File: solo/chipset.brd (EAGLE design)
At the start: 41 x 15 mm, 24 parts

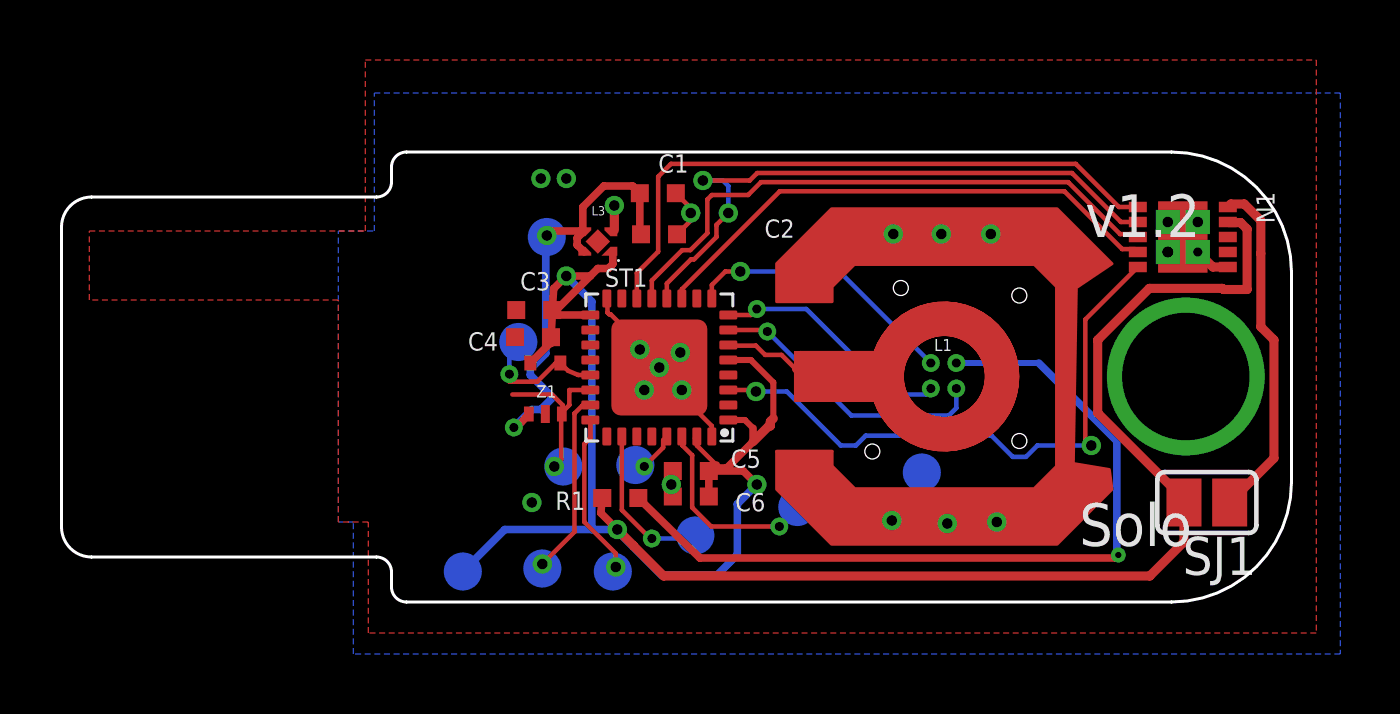
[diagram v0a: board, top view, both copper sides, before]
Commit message: add molex nfc antenna/coil
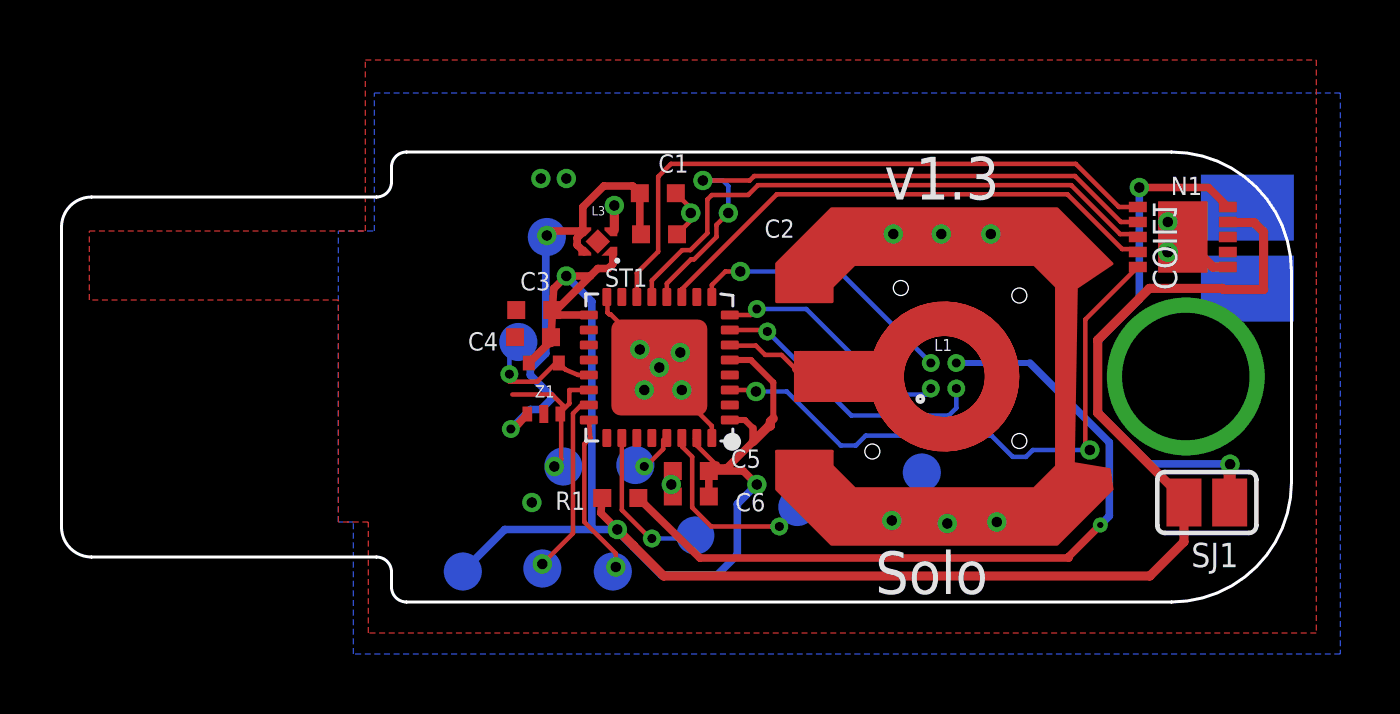
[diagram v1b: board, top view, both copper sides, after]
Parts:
- added COIL1: MOLEX_NFC_COIL_1462360101, efm-fido:MOLEX_NFC_COIL1
- moved Z1 0.05 mm to (50.5, 53.0)
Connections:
- new net N$12: N1.P$4
- new net N$13: N1.P$3
- net PE: no longer N1.P$12, N1.P$13, N1.P$14, N1.P$15
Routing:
- net N$7: track 11.6 -> 17.7 mm, vias 0 -> 2
- net N$6: track 27.2 -> 25.9 mm
- net +3V3: track 80.0 -> 80.9 mm
- net PE: track 18.6 -> 18.7 mm, vias 21 -> 20
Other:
- board text added: "v1.3"
- board text removed: "v1.2"

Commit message: update chipset
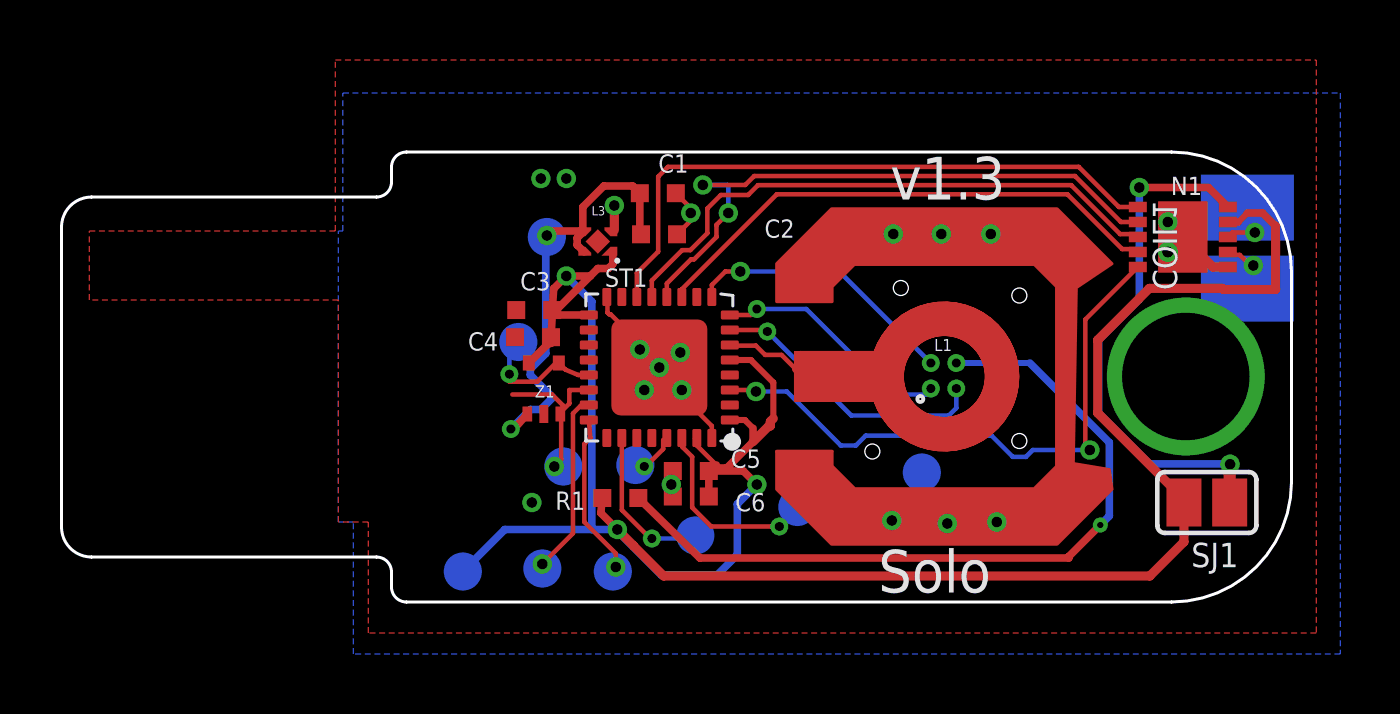
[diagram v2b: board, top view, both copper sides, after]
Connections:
- net N$12: now also COIL1.P$2
- net N$13: now also COIL1.P$1
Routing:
- net N$13: track 0.00 -> 1.90 mm, vias 0 -> 1
- net N$12: track 0.00 -> 1.89 mm, vias 0 -> 1
- net +3V3: track 80.9 -> 82.1 mm
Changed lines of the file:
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@@
 <plain>
 <wire x1="74.05" y1="54.25" x2="35.1" y2="54.25" width="0.1524" layer="49"/>
-<text x="62.1" y="47" size="1.4224" layer="21">Solo</text>
-<text x="62.4" y="60.15" size="1.4224" layer="21">v1.3</text>
+<text x="62.2" y="47.05" size="1.4224" layer="21">Solo</text>
+<text x="62.6" y="60.15" size="1.4224" layer="21">v1.3</text>
 <hole x="62" y="51.75" drill="0.5"/>
 <wire x1="35" y1="59.3" x2="45.9" y2="59.3" width="0.2" layer="47"/>
@@
 <vertex x="35.9" y="56.8"/>
 <vertex x="35.9" y="59.1"/>
-<vertex x="45.1" y="59.1"/>
-<vertex x="45.1" y="64.8"/>
+<vertex x="44.1" y="59.1"/>
+<vertex x="44.1" y="64.8"/>
 <vertex x="76.8" y="64.8"/>
-<vertex x="76.8" y="57.5"/>
 <vertex x="76.8" y="45.7"/>
 <vertex x="45.2" y="45.7"/>
@@
 <polygon width="0.1016" layer="16">
 <vertex x="44.2" y="59.1"/>
-<vertex x="45.4" y="59.1"/>
-<vertex x="45.4" y="63.7"/>
+<vertex x="44.35" y="59.1"/>
+<vertex x="44.35" y="63.7"/>
 <vertex x="77.6" y="63.7"/>
 <vertex x="77.6" y="45"/>
@@
 <wire x1="71.25" y1="47.6" x2="72.388" y2="48.738" width="0.3048" layer="1"/>
 <wire x1="72.388" y1="48.738" x2="72.388" y2="50.05" width="0.3048" layer="1"/>
-<wire x1="73.8702" y1="59.3798" x2="74.72625" y2="59.3798" width="0.3048" layer="1"/>
-<wire x1="74.72625" y1="59.3798" x2="75.0428" y2="59.06325" width="0.3048" layer="1"/>
-<wire x1="75.0428" y1="59.06325" x2="75.0428" y2="57.15" width="0.3048" layer="1"/>
+<wire x1="75.4428" y1="59.26325" x2="75.4428" y2="57.15" width="0.3048" layer="1"/>
 <wire x1="73.66688125" y1="57.1878" x2="71.23311875" y2="57.1878" width="0.3048" layer="1"/>
 <wire x1="71.23311875" y1="57.1878" x2="69.5122" y2="55.46688125" width="0.3048" layer="1"/>
 <wire x1="69.5122" y1="55.46688125" x2="69.5122" y2="53.03311875" width="0.3048" layer="1"/>
-<wire x1="75.0428" y1="57.15" x2="73.70468125" y2="57.15" width="0.3048" layer="1"/>
+<wire x1="75.4428" y1="57.15" x2="73.70468125" y2="57.15" width="0.3048" layer="1"/>
 <wire x1="73.70468125" y1="57.15" x2="73.66688125" y2="57.1878" width="0.3048" layer="1"/>
 <wire x1="72.388" y1="50.15731875" x2="72.388" y2="50.05" width="0.3048" layer="1"/>
 <wire x1="69.5122" y1="53.03311875" x2="72.388" y2="50.15731875" width="0.3048" layer="1"/>
-<wire x1="73.85" y1="59.4" x2="73.8702" y2="59.3798" width="0.1524" layer="1"/>
+<wire x1="73.85" y1="59.4" x2="73.8798" y2="59.4298" width="0.254" layer="1"/>
+<wire x1="73.85" y1="59.4" x2="74.2" y2="59.4" width="0.254" layer="1"/>
+<wire x1="74.2" y1="59.4" x2="74.5" y2="59.7" width="0.2032" layer="1"/>
+<wire x1="74.5" y1="59.7" x2="75.00605" y2="59.7" width="0.254" layer="1"/>
+<wire x1="75.00605" y1="59.7" x2="75.4428" y2="59.26325" width="0.254" layer="1"/>
 </signal>
 <signal name="N$6">
@@
 <wire x1="70.7536" y1="58.9964" x2="70.2597125" y2="58.9964" width="0.1524" layer="1"/>
 <wire x1="70.2597125" y1="58.9964" x2="68.6279125" y2="60.6282" width="0.1524" layer="1"/>
-<wire x1="57.861175" y1="60.3" x2="56.65" y2="60.3" width="0.1524" layer="1"/>
-<wire x1="56.65" y1="60.3" x2="56.5" y2="60.15" width="0.1524" layer="1"/>
+<wire x1="57.861175" y1="60.3" x2="56.95" y2="60.3" width="0.1524" layer="1"/>
+<wire x1="56.95" y1="60.3" x2="56.5" y2="59.85" width="0.1524" layer="1"/>
 <wire x1="58.189375" y1="60.6282" x2="57.861175" y2="60.3" width="0.1524" layer="1"/>
 <wire x1="55.9346875" y1="58.4614" x2="55.6614" y2="58.4614" width="0.1524" layer="1"/>
 <wire x1="56.5" y1="59.0267125" x2="55.9346875" y2="58.4614" width="0.1524" layer="1"/>
 <wire x1="54.65" y1="57.45" x2="54.65" y2="56.9" width="0.1524" layer="1"/>
-<wire x1="56.5" y1="60.15" x2="56.5" y2="59.0267125" width="0.1524" layer="1"/>
+<wire x1="56.5" y1="59.85" x2="56.5" y2="59.0267125" width="0.1524" layer="1"/>
 <wire x1="55.6614" y1="58.4614" x2="54.65" y2="57.45" width="0.1524" layer="1"/>
 </signal>
@@
 <wire x1="70.28716875" y1="59.4" x2="68.75416875" y2="60.933" width="0.1524" layer="1"/>
 <wire x1="68.75416875" y1="60.933" x2="58.06311875" y2="60.933" width="0.1524" layer="1"/>
-<wire x1="58.06311875" y1="60.933" x2="57.91431875" y2="60.7842" width="0.1524" layer="1"/>
-<wire x1="57.91431875" y1="60.7842" x2="56.3512875" y2="60.7842" width="0.1524" layer="1"/>
-<via x="56.3512875" y="60.7842" extent="1-16" drill="0.35"/>
-<wire x1="56.3512875" y1="60.7842" x2="57.0158" y2="60.7842" width="0.1524" layer="16"/>
-<wire x1="57.0158" y1="60.7842" x2="57.2" y2="60.6" width="0.1524" layer="16"/>
+<wire x1="58.06311875" y1="60.933" x2="57.76431875" y2="60.6342" width="0.1524" layer="1"/>
+<wire x1="57.76431875" y1="60.6342" x2="56.3512875" y2="60.6342" width="0.1524" layer="1"/>
+<via x="56.3512875" y="60.6342" extent="1-16" drill="0.35"/>
+<wire x1="56.3512875" y1="60.6342" x2="57.1658" y2="60.6342" width="0.1524" layer="16"/>
+<wire x1="57.1658" y1="60.6342" x2="57.2" y2="60.6" width="0.1524" layer="16"/>
 <wire x1="57.2" y1="60.6" x2="57.2" y2="59.7" width="0.1524" layer="16"/>
 <via x="57.2" y="59.7" extent="1-16" drill="0.35"/>
@@
 <contactref element="ST1" pad="14"/>
 <wire x1="70.85" y1="59.9" x2="70.218225" y2="59.9" width="0.1524" layer="1"/>
-<wire x1="68.780425" y1="61.3378" x2="70.218225" y2="59.9" width="0.1524" layer="1"/>
+<wire x1="68.880425" y1="61.2378" x2="70.218225" y2="59.9" width="0.1524" layer="1"/>
 <wire x1="54.15" y1="57.7" x2="54.15" y2="56.9" width="0.1524" layer="1"/>
 <wire x1="54.15" y1="57.7" x2="54.8614" y2="58.4114" width="0.1524" layer="1"/>
 <wire x1="54.8614" y1="58.4114" x2="54.8614" y2="60.9114" width="0.1524" layer="1"/>
-<wire x1="54.8614" y1="60.9114" x2="55.2878" y2="61.3378" width="0.1524" layer="1"/>
-<wire x1="55.2878" y1="61.3378" x2="68.780425" y2="61.3378" width="0.1524" layer="1"/>
+<wire x1="54.8614" y1="60.9114" x2="55.1878" y2="61.2378" width="0.1524" layer="1"/>
+<wire x1="55.1878" y1="61.2378" x2="68.880425" y2="61.2378" width="0.1524" layer="1"/>
 </signal>
 <signal name="N$12">
 <contactref element="N1" pad="P$4"/>
+<contactref element="COIL1" pad="P$2"/>
+<via x="74.7" y="57.95" extent="1-16" drill="0.35"/>
+<wire x1="73.85" y1="58.4" x2="73.9464" y2="58.3036" width="0.1524" layer="1"/>
+<wire x1="73.9464" y1="58.3036" x2="74.2446875" y2="58.3036" width="0.1524" layer="1"/>
+<wire x1="74.65" y1="58" x2="74.7" y2="57.95" width="0.1524" layer="1"/>
+<wire x1="74.65" y1="58" x2="74.5482875" y2="58" width="0.1524" layer="1"/>
+<wire x1="74.2446875" y1="58.3036" x2="74.5482875" y2="58" width="0.1524" layer="1"/>
+<wire x1="74.7" y1="57.95" x2="74.65" y2="57.9" width="0.1524" layer="16"/>
+<wire x1="74.65" y1="57.9" x2="74.65" y2="57.33" width="0.1524" layer="16"/>
+<wire x1="74.65" y1="57.33" x2="74.5" y2="57.18" width="0.1524" layer="16"/>
 </signal>
 <signal name="N$13">
 <contactref element="N1" pad="P$3"/>
+<contactref element="COIL1" pad="P$1"/>
+<wire x1="74.75" y1="59.05" x2="74" y2="59.05" width="0.1524" layer="1"/>
+<wire x1="73.85" y1="58.9" x2="74" y2="59.05" width="0.1524" layer="1"/>
+<via x="74.75" y="59.05" extent="1-16" drill="0.35"/>
+<wire x1="74.75" y1="59.05" x2="74.5" y2="59.3" width="0.1524" layer="16"/>
+<wire x1="74.5" y1="59.3" x2="74.5" y2="59.88" width="0.1524" layer="16"/>
 </signal>
 </signals>
